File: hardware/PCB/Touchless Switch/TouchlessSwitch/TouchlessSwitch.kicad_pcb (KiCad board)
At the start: 2 copper layers, 63.4 x 53 mm, 12 parts, among them K1 Screw_Terminal_01x02, K2 Screw_Terminal_01x02, K3 Conn_02x20_Odd_Even, T1 BC337

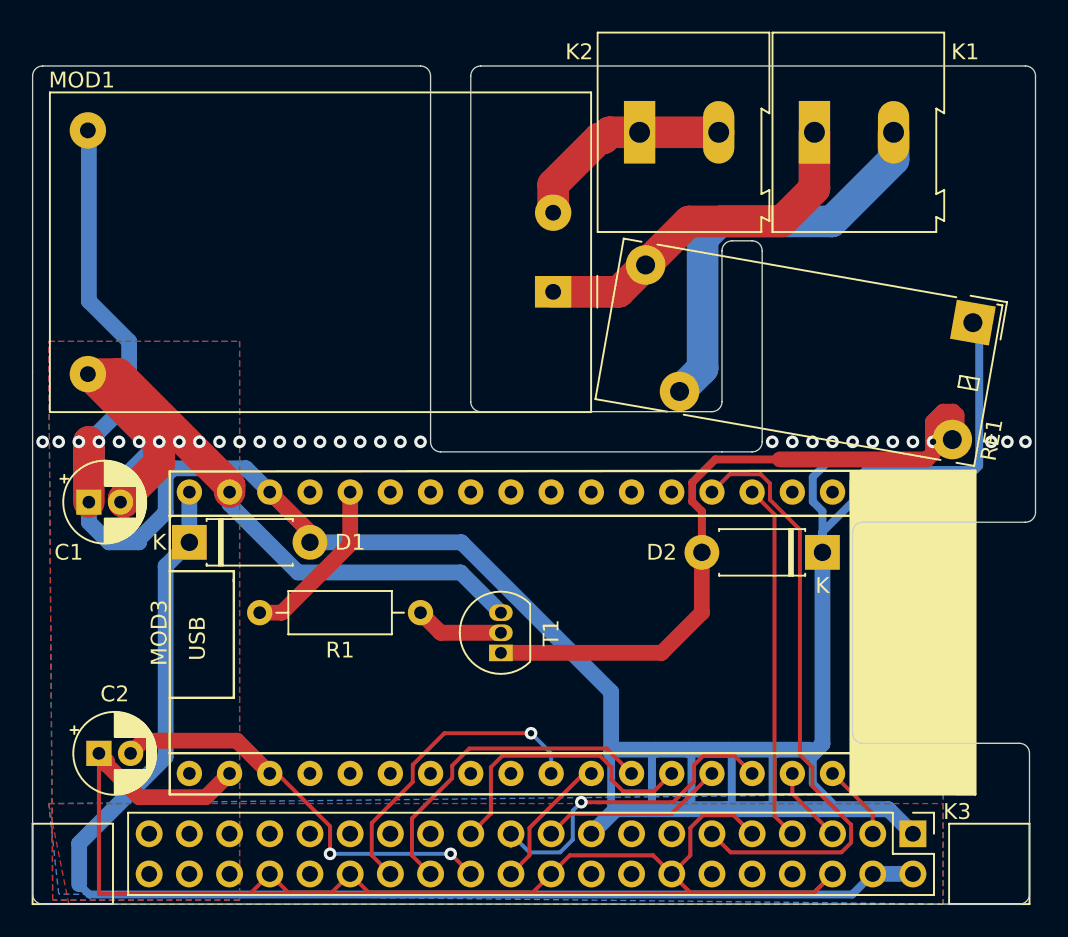
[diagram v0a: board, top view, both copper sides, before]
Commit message: PCB Files Update for latching relay
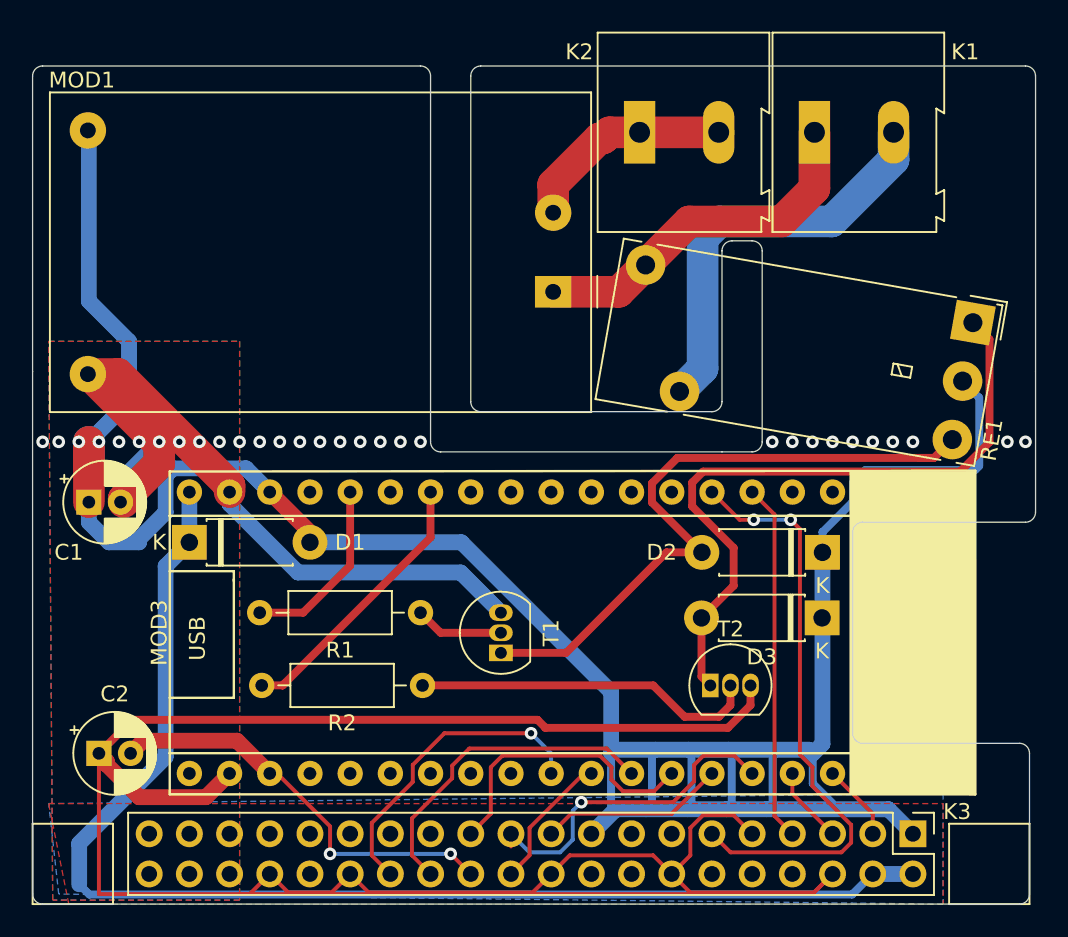
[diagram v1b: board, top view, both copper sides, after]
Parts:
- added D3: 1N4001, Diode_THT:D_DO-41_SOD81_P7.62mm_Horizontal, F.Cu at (196.2, 140.7)
- added R2: 1kR, Resistor_THT:R_Axial_DIN0207_L6.3mm_D2.5mm_P10.16mm_Horizontal, F.Cu at (170.9, 144.9)
- added T2: BC337, Package_TO_SOT_THT:TO-92_Inline, F.Cu at (189.1, 144.9)
- D2: value D -> 1N4001
- K3: value Conn_02x20_Odd_Even -> Pinheader
- RE1: value ADW11 -> ADW1203HLW; footprint Relay_THT:Relay_1P1T_NO_10x24x18.8mm_Panasonic_ADW11xxxxW_THT -> ADW1203HLW:Relay_1P1T_NO_10x24x18.8mm_Panasonic_ADW11xxxxW_THT
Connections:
- net RE_OUT renamed RE_R_OUT
- K3 pad 10: Net-(K3-Pad10) -> unconnected-(K3-Pad10)
- K3 pad 12: Net-(K3-Pad12) -> unconnected-(K3-Pad12)
- K3 pad 13: Net-(K3-Pad13) -> unconnected-(K3-Pad13)
- K3 pad 15: Net-(K3-Pad15) -> unconnected-(K3-Pad15)
- K3 pad 16: Net-(K3-Pad16) -> unconnected-(K3-Pad16)
- K3 pad 18: Net-(K3-Pad18) -> unconnected-(K3-Pad18)
- K3 pad 27: Net-(K3-Pad27) -> unconnected-(K3-Pad27)
- K3 pad 29: Net-(K3-Pad29) -> unconnected-(K3-Pad29)
- K3 pad 31: Net-(K3-Pad31) -> unconnected-(K3-Pad31)
- K3 pad 32: Net-(K3-Pad32) -> unconnected-(K3-Pad32)
- K3 pad 33: Net-(K3-Pad33) -> unconnected-(K3-Pad33)
- K3 pad 35: Net-(K3-Pad35) -> unconnected-(K3-Pad35)
- K3 pad 36: Net-(K3-Pad36) -> unconnected-(K3-Pad36)
- K3 pad 37: Net-(K3-Pad37) -> unconnected-(K3-Pad37)
- K3 pad 38: Net-(K3-Pad38) -> unconnected-(K3-Pad38)
- K3 pad 39: Net-(K3-Pad39) -> unconnected-(K3-Pad39)
- K3 pad 40: Net-(K3-Pad40) -> unconnected-(K3-Pad40)
- K3 pad 8: Net-(K3-Pad8) -> unconnected-(K3-Pad8)
- MOD3 pad 1: Net-(MOD3-Pad1) -> unconnected-(MOD3-Pad1)
- MOD3 pad 10: Net-(MOD3-Pad10) -> unconnected-(MOD3-Pad10)
- MOD3 pad 11: Net-(MOD3-Pad11) -> unconnected-(MOD3-Pad11)
- MOD3 pad 12: Net-(MOD3-Pad12) -> unconnected-(MOD3-Pad12)
- MOD3 pad 13: Net-(MOD3-Pad13) -> unconnected-(MOD3-Pad13)
- MOD3 pad 14: Net-(MOD3-Pad14) -> RE_S_OUT
- MOD3 pad 15: Net-(MOD3-Pad15) -> unconnected-(MOD3-Pad15)
- MOD3 pad 17: Net-(MOD3-Pad17) -> unconnected-(MOD3-Pad17)
- MOD3 pad 2: Net-(MOD3-Pad2) -> unconnected-(MOD3-Pad2)
- MOD3 pad 21: Net-(MOD3-Pad21) -> unconnected-(MOD3-Pad21)
- MOD3 pad 24: Net-(MOD3-Pad24) -> unconnected-(MOD3-Pad24)
- MOD3 pad 25: Net-(MOD3-Pad25) -> unconnected-(MOD3-Pad25)
- MOD3 pad 26: Net-(MOD3-Pad26) -> unconnected-(MOD3-Pad26)
- MOD3 pad 27: Net-(MOD3-Pad27) -> unconnected-(MOD3-Pad27)
- MOD3 pad 28: Net-(MOD3-Pad28) -> unconnected-(MOD3-Pad28)
- MOD3 pad 29: Net-(MOD3-Pad29) -> unconnected-(MOD3-Pad29)
- MOD3 pad 3: Net-(MOD3-Pad3) -> unconnected-(MOD3-Pad3)
- MOD3 pad 38: Net-(MOD3-Pad38) -> unconnected-(MOD3-Pad38)
- MOD3 pad 39: Net-(MOD3-Pad39) -> unconnected-(MOD3-Pad39)
- MOD3 pad 4: Net-(MOD3-Pad4) -> unconnected-(MOD3-Pad4)
- MOD3 pad 40: Net-(MOD3-Pad40) -> unconnected-(MOD3-Pad40)
- MOD3 pad 5: Net-(MOD3-Pad5) -> unconnected-(MOD3-Pad5)
- MOD3 pad 8: Net-(MOD3-Pad8) -> unconnected-(MOD3-Pad8)
- MOD3 pad 9: Net-(MOD3-Pad9) -> unconnected-(MOD3-Pad9)
- RE1 pad 1: 3V3_IN -> Net-(D3-Pad2)
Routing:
- net RE_S_OUT: track 0.00 -> 48.4 mm
- net GND_IN: track 169.5 -> 213.7 mm
- net Net-(D3-Pad2): track 0.00 -> 43.4 mm
- net Net-(R2-Pad1): track 0.00 -> 21.8 mm
- net 3V3_IN: track 184.9 -> 175.1 mm
- net RE_R_OUT: track 10.8 -> 16.2 mm
- net Net-(D2-Pad2): track 45.7 -> 42.0 mm, vias 2 -> 0
- net MGC_RST: track 38.7 -> 37.2 mm, vias 0 -> 2
- net (no net): vias 23 -> 22
